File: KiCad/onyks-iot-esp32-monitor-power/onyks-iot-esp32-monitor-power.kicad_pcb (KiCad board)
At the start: 2 copper layers, 36 parts, among them J1 Uart_con, J2 Jtag_con, J3 Conn_01x06, J4 Screw_Terminal_01x01, J5 Screw_Terminal_01x01, J6 Screw_Terminal_01x02, J7 Conn_01x02, Q1 SS8050, Q2 SS8050, SW1 reset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

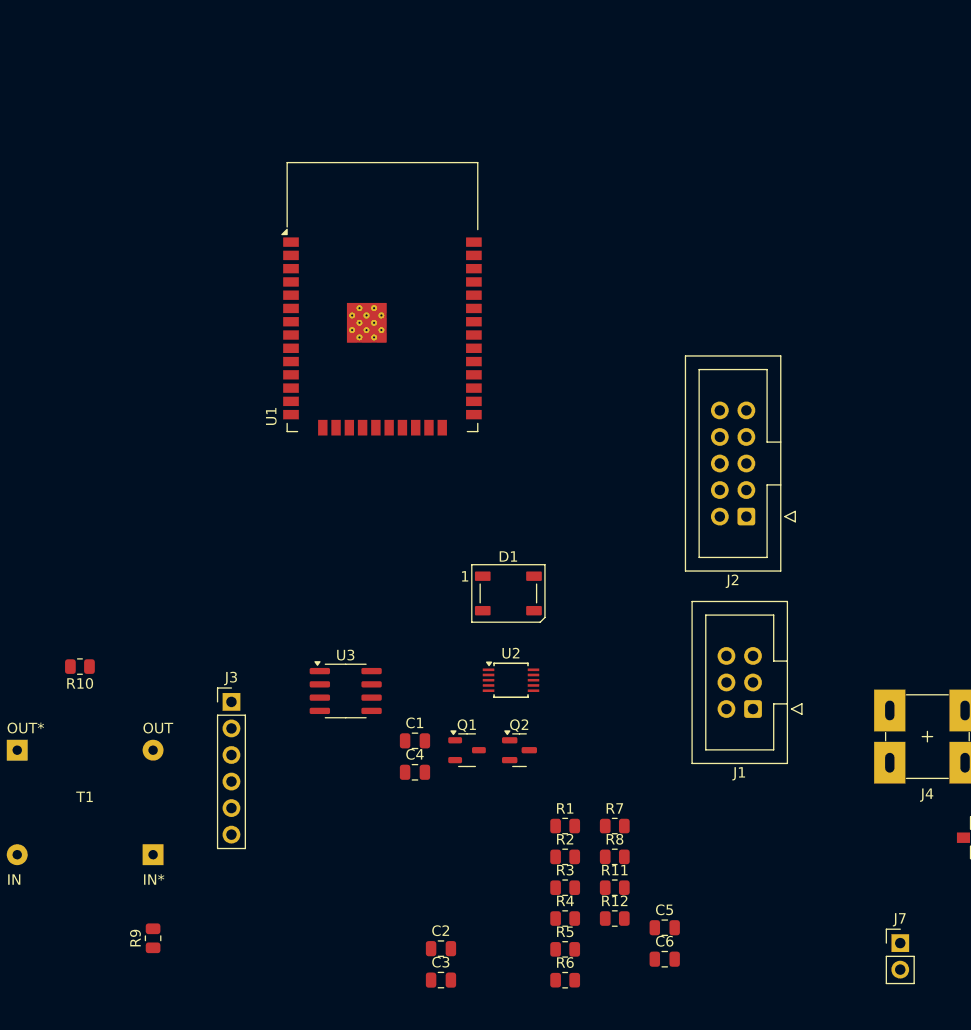
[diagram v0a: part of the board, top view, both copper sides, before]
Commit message: Add relay to sheme (not ended)
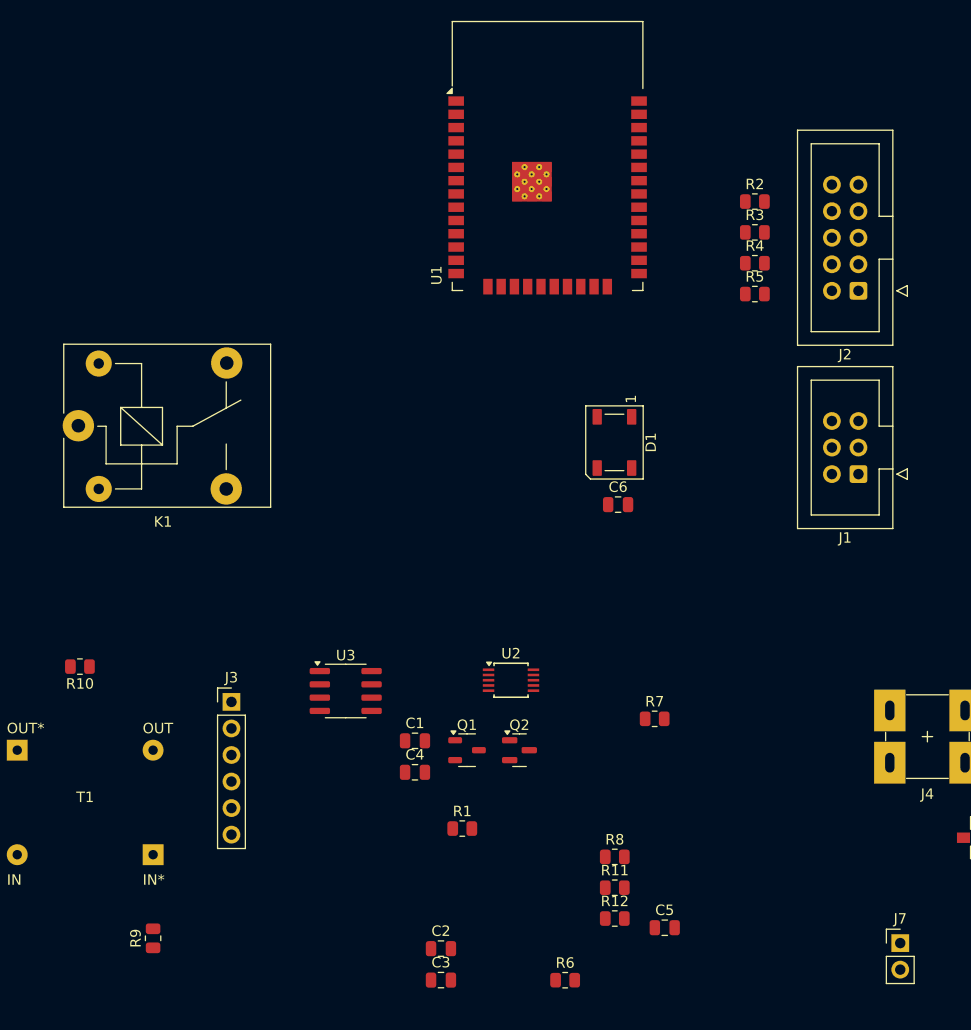
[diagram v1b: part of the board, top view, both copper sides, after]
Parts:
- added K1: SANYOU_SRD_Form_C, Relay_THT:Relay_SPDT_SANYOU_SRD_Series_Form_C, F.Cu at (104.3, 72.0)
- moved R2 65.3 mm to (169.1, 50.5)
- moved R3 65.3 mm to (169.1, 53.5)
- moved R4 65.3 mm to (169.1, 56.4)
- moved R5 65.3 mm to (169.1, 59.4)
- moved C6 43.7 mm to (156.0, 79.5)
- moved J1 24.6 mm to (179.0, 76.6)
- moved J2 24.1 mm to (179.0, 59.0)
- moved U1 20.8 mm to (149.2, 49.1)
- moved D1 17.7 mm to (155.7, 73.5), turned to -90 degrees
- moved R7 10.9 mm to (159.5, 100.0)
- moved R1 9.85 mm to (141.1, 110.5)
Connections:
- net Net-(J7-Pin_2) renamed +5V

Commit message: Add relay and 5x extra free GPIO; sheme V1.1
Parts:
- added D2: D, Diode_SMD:D_SMA, F.Cu at (23.5, 102.7)
- added D3: LED, LED_SMD:LED_0603_1608Metric, F.Cu at (49.4, 103.5)
- added J10: PAD, TestPoint:TestPoint_Pad_D1.0mm, F.Cu at (99.7, 238.1)
- added J11: PAD, TestPoint:TestPoint_Pad_D1.0mm, F.Cu at (104.1, 231.4)
- added J12: PAD, TestPoint:TestPoint_Pad_D1.0mm, F.Cu at (104.1, 234.9)
- added J13: PAD, TestPoint:TestPoint_Pad_D1.0mm, F.Cu at (104.1, 238.5)
- added J14: +3V3_PAD, TestPoint:TestPoint_Pad_D1.5mm, F.Cu at (87.6, -13.3)
- added J15: +5V_PAD, TestPoint:TestPoint_Pad_D1.5mm, F.Cu at (87.6, -9.79)
- added J16: ~, macmysz:CONN_03x05, F.Cu at (55.9, 26.7)
- added J8: Screw_Terminal_01x03, TerminalBlock:TerminalBlock_bornier-3_P5.08mm, F.Cu at (22.7, 95.9)
- added J9: UART2, Connector_PinHeader_2.54mm:PinHeader_1x03_P2.54mm_Vertical, F.Cu at (155.6, 54.0)
- added JP1: IF_NOT_USED, Jumper:SolderJumper-2_P1.3mm_Open_RoundedPad1.0x1.5mm, F.Cu at (94.6, 242.6)
- added JP2: IF_NOT_USED, Jumper:SolderJumper-2_P1.3mm_Open_RoundedPad1.0x1.5mm, F.Cu at (94.6, 246.1)
- added JP3: JUMPER_3V3/5V, Jumper:SolderJumper-3_P1.3mm_Bridged12_RoundedPad1.0x1.5mm, F.Cu at (58.4, 17.1)
- added Q3: MMBT2222A, Package_TO_SOT_SMD:SOT-23, F.Cu at (41.9, 102.2)
- added R13: 470, Resistor_SMD:R_0805_2012Metric, F.Cu at (29.8, 101.9)
- added R14: 1K, Resistor_SMD:R_0805_2012Metric, F.Cu at (29.8, 104.9)
- J3: value Conn_01x06 -> UART_ONYKS
- J4: value Screw_Terminal_01x01 -> I_SENS_IN
- J5: value Screw_Terminal_01x01 -> I_SENS_OUT
- J6: value Screw_Terminal_01x02 -> MAIN_VOLTAGE_INPUT
- moved C7 158.2 mm to (98.1, -8.12)
- moved U4 158.2 mm to (98.5, -1.21)
- moved C8 158.2 mm to (98.1, -5.12)
- moved J7 158.2 mm to (85.1, -2.80)
- moved C4 154.5 mm to (96.6, 254.3)
- moved U2 154.5 mm to (105.8, 245.5)
- moved SW1 101.9 mm to (112.4, 48.9)
- moved J3 101.5 mm to (33.3, 152.9)
- moved R12 101.5 mm to (70.0, 173.6)
- moved Q1 101.5 mm to (55.9, 157.5)
- moved Q2 101.5 mm to (60.9, 157.5)
- moved R11 101.5 mm to (70.0, 170.6)
- moved U3 98.2 mm to (227.7, 87.7)
- moved C5 86.1 mm to (239.7, 86.4)
- moved R10 79.7 mm to (161.4, 150.8)
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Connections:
- K1 pad 1: unconnected-(K1-Pad1) -> Net-(J8-Pin_2)
- K1 pad 2: unconnected-(K1-Pad2) -> Net-(D2-A)
- K1 pad 3: unconnected-(K1-Pad3) -> Net-(J8-Pin_3)
- K1 pad 4: unconnected-(K1-Pad4) -> Net-(J8-Pin_1)
- K1 pad 5: unconnected-(K1-Pad5) -> +5V
- U1 pad 10: unconnected-(U1-IO25-Pad10) -> /FOUT3
- U1 pad 11: unconnected-(U1-IO26-Pad11) -> /FOUT4
- U1 pad 12: unconnected-(U1-IO27-Pad12) -> /FOUT5
- U1 pad 26: unconnected-(U1-IO4-Pad26) -> /RELAY
- U1 pad 27: unconnected-(U1-IO16-Pad27) -> Net-(J9-Pin_1)
- U1 pad 28: unconnected-(U1-IO17-Pad28) -> Net-(J9-Pin_2)
- U1 pad 8: unconnected-(U1-IO32-Pad8) -> /FOUT1
- U1 pad 9: unconnected-(U1-IO33-Pad9) -> /FOUT2

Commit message: start editing pcb
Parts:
- removed R2, R3, R4, R5: 100R, Resistor_SMD:R_0805_2012Metric
- added RN1: 100, Resistor_SMD:R_Array_Concave_4x0603, F.Cu at (169.0, 47.9)
- moved C4 193.8 mm to (158.0, 70.5)
- moved JP2 184.4 mm to (158.0, 72.9)
- moved U2 180.0 mm to (147.8, 70.5)
- moved JP1 178.7 mm to (158.0, 75.4)
- moved J10 173.6 mm to (140.8, 69.5)
- moved J13 173.1 mm to (154.7, 72.9)
- moved J12 167.6 mm to (154.7, 75.2)
- moved J11 163.9 mm to (140.8, 71.6)
- moved J3 158.2 mm to (168.9, 71.4), turned to 180 degrees
- moved Q1 146.1 mm to (163.7, 58.9), turned to 180 degrees
- moved R12 145.7 mm to (164.7, 62.9), turned to -90 degrees
- moved R11 141.9 mm to (162.3, 62.9), turned to 90 degrees
- moved Q2 136.9 mm to (163.4, 66.8), turned to 180 degrees
- moved D2 113.3 mm to (132.8, 72.8), turned to 180 degrees
- moved J8 111.4 mm to (134.0, 101.6), turned to 180 degrees
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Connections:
- J10 pad 1: /A1 -> /A0
- J11 pad 1: /A2 -> /A1
- J12 pad 1: /A3 -> /A2
- J13 pad 1: /A4 -> /A3
- JP1 pad 1: /A3 -> /A2
- JP2 pad 1: /A4 -> /A3
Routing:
- net +3V3: track 0.00 -> 102.6 mm, vias 0 -> 2
- net +5V: track 0.00 -> 17.1 mm
- net /EN: track 0.00 -> 14.5 mm, vias 0 -> 2
- net Net-(JP3-C): track 0.00 -> 13.2 mm
- net /FOUT4: track 0.00 -> 1.25 mm, vias 0 -> 1
- net /FOUT3: track 0.00 -> 1.25 mm, vias 0 -> 1
- net /FOUT2: track 0.00 -> 1.25 mm, vias 0 -> 1
- net /FOUT1: track 0.00 -> 1.25 mm, vias 0 -> 1
- net /FOUT5: track 0.00 -> 1.25 mm, vias 0 -> 1

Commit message: edit pcb
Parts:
- removed JP3: JUMPER_3V3/5V, Jumper:SolderJumper-3_P1.3mm_Bridged12_RoundedPad1.0x1.5mm
- added J17: Ground, Connector_Wire:SolderWire-2sqmm_1x01_D2mm_OD3.9mm, F.Cu at (180.3, 86.4)
- J16: value ~ -> FOUT_conn; footprint macmysz:CONN_03x05 -> Connector_PinSocket_2.54mm:PinSocket_1x08_P2.54mm_Vertical
- moved R9 18.2 mm to (164.6, 86.4), turned to -90 degrees
- moved J10 13.7 mm to (153.2, 63.5)
- moved J11 13.7 mm to (153.2, 65.7)
- moved R10 13.5 mm to (157.0, 74.9)
- moved J15 13.3 mm to (134.5, 57.7)
- moved J14 11.3 mm to (139.6, 57.7)
- moved J7 10.2 mm to (131.4, 63.8)
- moved U4 10.0 mm to (138.4, 62.1)
- moved C7 10.0 mm to (134.6, 62.1)
- moved C8 10.0 mm to (142.1, 62.2)
- moved D2 8.91 mm to (141.7, 72.1)
- moved D3 8.91 mm to (140.3, 68.6)
- moved R13 8.91 mm to (136.2, 68.6)
- moved R14 8.91 mm to (131.7, 68.6)
- moved Q3 8.89 mm to (131.8, 72.9)
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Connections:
- J16 pad 2: Net-(JP3-C) -> /FOUT2
- J16 pad 3: GND -> /FOUT3
- J16 pad 4: /FOUT2 -> /FOUT4
- J16 pad 5: Net-(JP3-C) -> /FOUT5
- J16 pad 7: /FOUT3 -> +3V3
- J16 pad 8: Net-(JP3-C) -> +5V
- RN1 pad 1: /MTDO -> /MTMS
- RN1 pad 2: /MTMS -> /MTCK
- RN1 pad 3: /MTCK -> /MTDO
- RN1 pad 6: Net-(RN1-R3.2) -> Net-(RN1C-R3.2)
- RN1 pad 7: Net-(RN1-R2.2) -> Net-(RN1B-R2.2)
- RN1 pad 8: Net-(RN1-R1.2) -> Net-(RN1A-R1.2)
- U1 pad 13: Net-(RN1-R2.2) -> Net-(RN1A-R1.2)
- U1 pad 16: Net-(RN1-R3.2) -> Net-(RN1B-R2.2)
- U1 pad 23: Net-(RN1-R1.2) -> Net-(RN1C-R3.2)
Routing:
- net +3V3: track 102.6 -> 150.0 mm
- net Net-(RN1D-R4.2): track 0.00 -> 31.5 mm, vias 0 -> 2
- net Net-(RN1A-R1.2): track 0.00 -> 28.6 mm, vias 0 -> 2
- net Net-(RN1B-R2.2): track 0.00 -> 28.2 mm, vias 0 -> 2
- net Net-(J8-Pin_2): track 0.00 -> 23.6 mm
- net Net-(J6-Pin_1): track 0.00 -> 23.3 mm
- net Net-(J6-Pin_2): track 0.00 -> 23.1 mm
- net Net-(RN1C-R3.2): track 0.00 -> 20.1 mm, vias 0 -> 2
- net /FOUT1: track 1.25 -> 19.4 mm
- net /BOOT: track 0.00 -> 16.4 mm
- net /RTS: track 0.00 -> 16.2 mm
- net /FOUT2: track 1.25 -> 16.8 mm
- net /EN: track 14.5 -> 29.6 mm, vias 2 -> 3
- net Net-(D2-A): track 0.00 -> 15.1 mm
- net /FOUT3: track 1.25 -> 14.7 mm
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- added copper zone on B.Cu, net Earth
- added copper zone on F.Cu, net Earth

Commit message: pcb finished
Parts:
- added REF**: MountingHole_3.2mm_M3, MountingHole:MountingHole_3.2mm_M3, F.Cu at (177.8, 78.2)
- added REF**: MountingHole_3.2mm_M3, MountingHole:MountingHole_3.2mm_M3, F.Cu at (154.4, 57.9)
- moved JP1 9.02 mm to (148.5, 72.5), turned to 180 degrees
- moved JP2 9.02 mm to (148.5, 70.0), turned to 180 degrees
- moved C4 8.93 mm to (148.8, 64.5), turned to -90 degrees
- moved J10 8.42 mm to (157.9, 70.5), turned to 180 degrees
- moved U2 7.16 mm to (153.7, 63.5), turned to 180 degrees
- moved J11 5.40 mm to (157.9, 68.3), turned to 180 degrees
- moved R10 3.50 mm to (160.1, 73.4)
- moved J12 2.62 mm to (151.8, 70.5)
- moved J13 2.57 mm to (151.8, 68.3)
- moved J9 2.03 mm to (163.8, 54.1)
- moved C5 0.38 mm to (170.8, 82.2)
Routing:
- net /EN: track 29.6 -> 99.6 mm, vias 3 -> 4
- net /ALERT: track 0.00 -> 47.5 mm, vias 0 -> 3
- net SCL: track 0.00 -> 42.6 mm, vias 0 -> 3
- net SDA: track 0.00 -> 40.2 mm, vias 0 -> 3
- net /RELAY: track 2.70 -> 41.3 mm, vias 0 -> 2
- net /TXD: track 10.6 -> 46.5 mm
- net /A0: track 0.00 -> 35.6 mm, vias 0 -> 2
- net /LED: track 0.00 -> 31.4 mm, vias 0 -> 2
- net /RXD: track 10.7 -> 41.6 mm
- net +3V3: track 150.0 -> 180.0 mm
- net /A1: track 0.00 -> 20.2 mm
- net /A2: track 0.00 -> 14.4 mm
- net +5V: track 29.0 -> 40.7 mm
- net /A3: track 0.00 -> 11.1 mm
- net /BOOT: track 16.4 -> 26.8 mm
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- added copper zone on B.Cu, net GND
- added copper zone on F.Cu, net GND
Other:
- board outline added: 54.9 x 72.1 mm
- board text added: "Designed by MACMYSZ"
- board text added: "ONYKS iot esp32 moitor power"

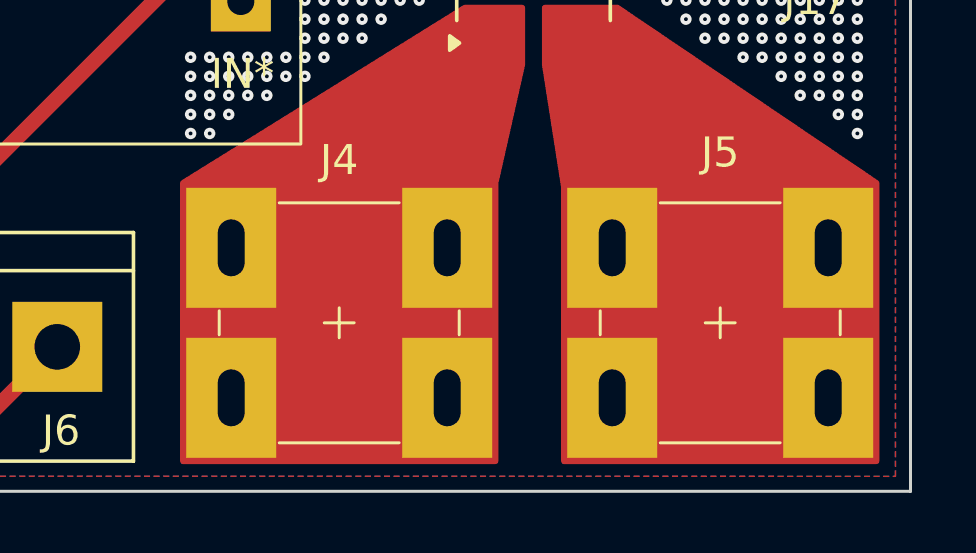
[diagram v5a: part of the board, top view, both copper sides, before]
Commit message: add Logo
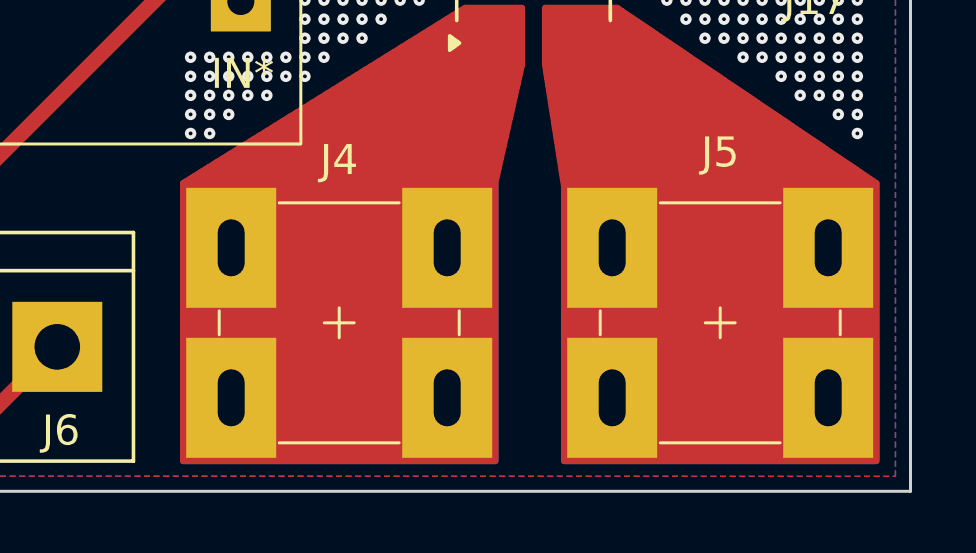
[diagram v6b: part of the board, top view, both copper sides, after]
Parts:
- added G***: LOGO, macmysz:logo, B.Cu at (138.6, 39.9)

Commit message: PCB update
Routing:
- net +3V3: track 180.0 -> 199.0 mm
- net +5V: track 40.7 -> 37.7 mm
- net Net-(D2-A): track 15.1 -> 16.0 mm
- net GND: vias 53 -> 126

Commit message: update PCB 2
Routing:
- net +5V: track 37.7 -> 41.3 mm
- net GND: vias 126 -> 123
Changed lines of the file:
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@@
 	)
 	(via
-		(at 141.859 66.421)
+		(at 141.605 66.421)
 		(size 0.381)
 		(drill 0.127)
@@
 	)
 	(via
-		(at 137.16 64.135)
-		(size 0.381)
-		(drill 0.127)
-		(layers "F.Cu" "B.Cu")
-		(free yes)
-		(net 1)
-	)
-	(via
 		(at 173.609 70.993)
 		(size 0.381)
@@
 	)
 	(via
-		(at 135.89 64.135)
-		(size 0.381)
-		(drill 0.127)
-		(layers "F.Cu" "B.Cu")
-		(free yes)
-		(net 1)
-	)
-	(via
 		(at 140.462 62.23)
 		(size 0.381)
@@
 	)
 	(via
-		(at 136.525 64.135)
-		(size 0.381)
-		(drill 0.127)
-		(layers "F.Cu" "B.Cu")
-		(free yes)
-		(net 1)
-	)
-	(via
 		(at 137.16 64.77)
 		(size 0.381)
@@
 	)
 	(segment
+		(start 138.364053 64.1255)
+		(end 136.3885 64.1255)
+		(width 0.508)
+		(layer "F.Cu")
+		(net 53)
+	)
+	(segment
 		(start 137.294427 61.155874)
 		(end 134.622874 61.155874)
@@
 	)
 	(segment
+		(start 134.559 61.214)
+		(end 134.5685 61.2235)
+		(width 1.016)
+		(layer "F.Cu")
+		(net 53)
+	)
+	(segment
+		(start 136.3885 64.1255)
+		(end 136.017 63.754)
+		(width 0.508)
+		(layer "F.Cu")
+		(net 53)
+	)
+	(segment
 		(start 134.62 57.785)
 		(end 134.493 57.658)
@@
 	)
 	(segment
-		(start 136.334874 63.055874)
-		(end 136.017 62.738)
+		(start 143.721909 72.136)
+		(end 143.721909 69.483356)
 		(width 0.508)
 		(layer "F.Cu")
@@
 	)
 	(segment
-		(start 134.493 57.404)
-		(end 131.445 54.356)
+		(start 133.731 61.214)
+		(end 134.559 61.214)
 		(width 1.016)
 		(layer "F.Cu")
@@
 	)
 	(segment
-		(start 136.017 62.738)
-		(end 136.017 61.155874)
-		(width 0.508)
+		(start 131.191 61.214)
+		(end 133.731 61.214)
+		(width 1.016)
 		(layer "F.Cu")
 		(net 53)
 	)
 	(segment
-		(start 143.721909 69.483356)
-		(end 143.721909 72.136)
+		(start 134.493 57.404)
+		(end 131.445 54.356)
+		(width 1.016)
+		(layer "F.Cu")
+		(net 53)
+	)
+	(segment
+		(start 136.017 62.738)
+		(end 136.017 61.155874)
 		(width 0.508)
 		(layer "F.Cu")
@@
 	)
 	(segment
-		(start 131.191 61.214)
-		(end 134.559 61.214)
-		(width 1.016)
+		(start 136.017 63.754)
+		(end 136.017 62.738)
+		(width 0.508)
 		(layer "F.Cu")
 		(net 53)
@@
 	)
 	(segment
+		(start 134.5685 61.2235)
+		(end 136.014126 61.2235)
+		(width 1.016)
+		(layer "F.Cu")
+		(net 53)
+	)
+	(segment
 		(start 143.714 79.444)
 		(end 143.714 72.143909)
@@
 	)
 	(segment
-		(start 137.294427 63.055874)
-		(end 136.334874 63.055874)
+		(start 143.721909 69.483356)
+		(end 138.364053 64.1255)
 		(width 0.508)
 		(layer "F.Cu")
@@
 	)
 	(segment
+		(start 136.017 63.055874)
+		(end 136.017 62.738)
+		(width 0.508)
+		(layer "F.Cu")
+		(net 53)
+	)
+	(segment
 		(start 134.62 61.153)
 		(end 134.62 57.785)
@@
 	(segment
 		(start 137.294427 63.055874)
-		(end 143.721909 69.483356)
+		(end 136.017 63.055874)
 		(width 0.508)
 		(layer "F.Cu")
